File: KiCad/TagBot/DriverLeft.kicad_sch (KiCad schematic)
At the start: 3 parts, among them U2 ZXBM5210-SP

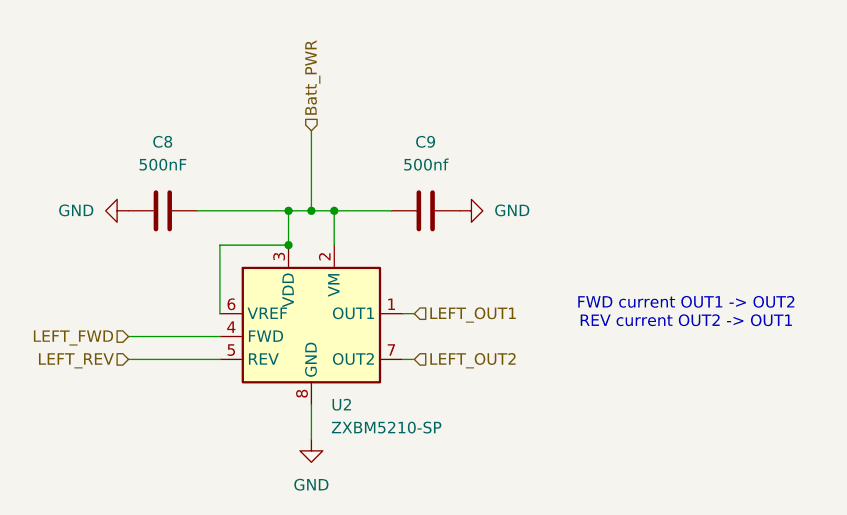
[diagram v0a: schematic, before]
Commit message: boot0 of stm32 connected to gnd
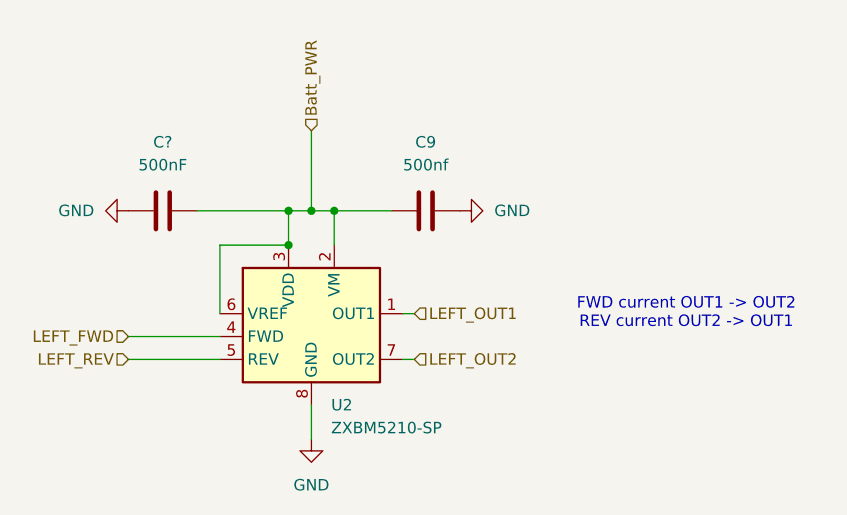
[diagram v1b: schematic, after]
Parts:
- renumbered C8 to C?
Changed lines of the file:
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@@
 		(dnp no)
 		(fields_autoplaced yes)
-		(property "Reference" "C8"
+		(property "Reference" "C?"
 			(at 124.46 66.04 90)
 			(effects
@@
 		)
 		(pin "1"
+		)
+		(instances
+			(project "TagBot"
+				(path "/6db08f37-7cb3-4000-93f1-ba0d0ffbeb19/3ab50834-de79-4373-bbc0-542f9f81e0c6"
+					(reference "C?")
+					(unit 1)
+				)
+			)
 		)
 	)
@@
 		(dnp no)
 		(fields_autoplaced yes)
-		(property "Reference" "#PWR019"
+		(property "Reference" "#PWR?"
 			(at 140.97 105.41 0)
 			(effects
@@
 		(pin "1"
 		)
-	)
+		(instances
+			(project "TagBot"
+				(path "/6db08f37-7cb3-4000-93f1-ba0d0ffbeb19/3ab50834-de79-4373-bbc0-542f9f81e0c6"
+					(reference "#PWR?")
+					(unit 1)
+				)
+			)
+		)
+	)

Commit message: update kicad
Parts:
- gave numbers to parts that had none: 1
- renumbered C9 to C202, U2 to U201
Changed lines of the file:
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@@
 	(generator "eeschema")
 	(generator_version "8.0")
-	(paper "A4")
+	(paper "A3")
 	(junction
 		(at 138.43 73.66)
@@
 		(dnp no)
 		(fields_autoplaced yes)
-		(property "Reference" "#PWR021"
+		(property "Reference" "#PWR0203"
 			(at 163.83 73.66 0)
 			(effects
@@
 			(project "TagBot"
 				(path "/6db08f37-7cb3-4000-93f1-ba0d0ffbeb19/3ab50834-de79-4373-bbc0-542f9f81e0c6"
-					(reference "#PWR021")
+					(reference "#PWR0203")
 					(unit 1)
 				)
@@
 		(dnp no)
 		(fields_autoplaced yes)
-		(property "Reference" "C?"
+		(property "Reference" "C201"
 			(at 124.46 66.04 90)
 			(effects
@@
 			(project "TagBot"
 				(path "/6db08f37-7cb3-4000-93f1-ba0d0ffbeb19/3ab50834-de79-4373-bbc0-542f9f81e0c6"
-					(reference "C?")
+					(reference "C201")
 					(unit 1)
 				)
@@
 		(dnp no)
 		(fields_autoplaced yes)
-		(property "Reference" "U2"
+		(property "Reference" "U201"
 			(at 143.1641 95.25 0)
 			(effects
@@
 			(project "TagBot"
 				(path "/6db08f37-7cb3-4000-93f1-ba0d0ffbeb19/3ab50834-de79-4373-bbc0-542f9f81e0c6"
-					(reference "U2")
+					(reference "U201")
 					(unit 1)
 				)
@@
 		(dnp no)
 		(fields_autoplaced yes)
-		(property "Reference" "#PWR020"
+		(property "Reference" "#PWR0201"
 			(at 114.3 73.66 0)
 			(effects
@@
 			(project "TagBot"
 				(path "/6db08f37-7cb3-4000-93f1-ba0d0ffbeb19/3ab50834-de79-4373-bbc0-542f9f81e0c6"
-					(reference "#PWR020")
+					(reference "#PWR0201")
 					(unit 1)
 				)
@@
 		(dnp no)
 		(fields_autoplaced yes)
-		(property "Reference" "C9"
+		(property "Reference" "C202"
 			(at 153.67 66.04 90)
 			(effects
@@
 			(project "TagBot"
 				(path "/6db08f37-7cb3-4000-93f1-ba0d0ffbeb19/3ab50834-de79-4373-bbc0-542f9f81e0c6"
-					(reference "C9")
+					(reference "C202")
 					(unit 1)
 				)
@@
 		(dnp no)
 		(fields_autoplaced yes)
-		(property "Reference" "#PWR?"
+		(property "Reference" "#PWR0202"
 			(at 140.97 105.41 0)
 			(effects
@@
 			(project "TagBot"
 				(path "/6db08f37-7cb3-4000-93f1-ba0d0ffbeb19/3ab50834-de79-4373-bbc0-542f9f81e0c6"
-					(reference "#PWR?")
+					(reference "#PWR0202")
 					(unit 1)
 				)

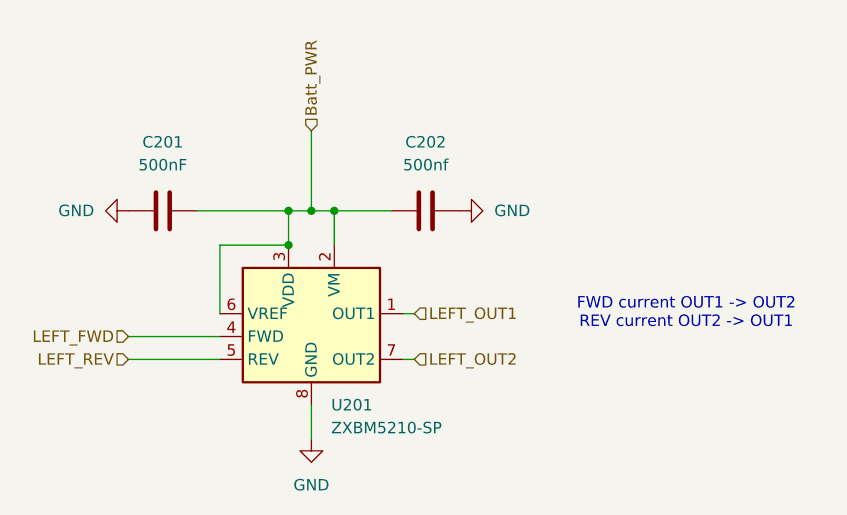
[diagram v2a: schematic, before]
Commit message: update footprint kicad
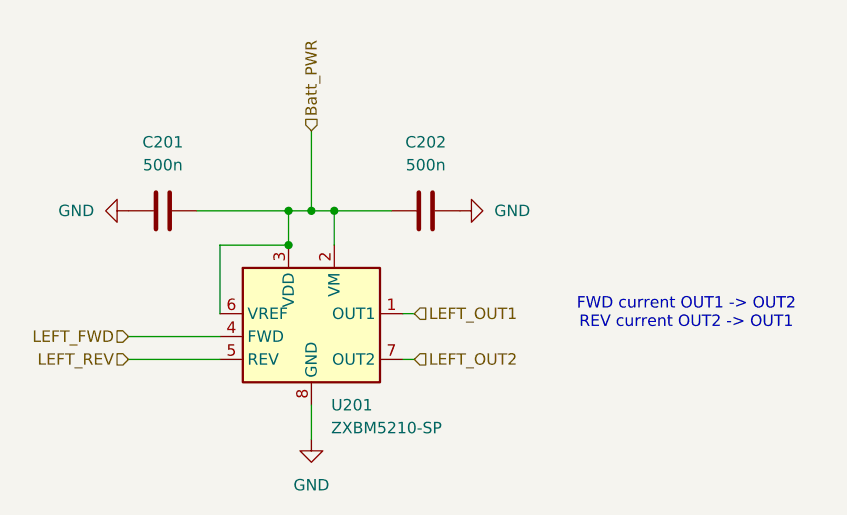
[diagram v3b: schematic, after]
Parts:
- C201: value 500nF -> 500n; footprint (none) -> Capacitor_SMD:C_0402_1005Metric
- C202: value 500nf -> 500n; footprint (none) -> Capacitor_SMD:C_0402_1005Metric
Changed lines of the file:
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@@
 			)
 		)
-		(property "Value" "500nF"
+		(property "Value" "500n"
 			(at 124.46 68.58 90)
 			(effects
@@
 			)
 		)
-		(property "Footprint" ""
+		(property "Footprint" "Capacitor_SMD:C_0402_1005Metric"
 			(at 128.27 72.6948 0)
 			(effects
@@
 			)
 		)
-		(property "Value" "500nf"
+		(property "Value" "500n"
 			(at 153.67 68.58 90)
 			(effects
@@
 			)
 		)
-		(property "Footprint" ""
+		(property "Footprint" "Capacitor_SMD:C_0402_1005Metric"
 			(at 149.86 74.6252 0)
 			(effects

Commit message: placement pcb
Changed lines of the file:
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@@
 		(color 0 0 0 0)
 	)
+	(junction
+		(at 143.51 76.2)
+		(diameter 0)
+		(color 0 0 0 0)
+	)
+	(wire
+		(pts
+			(xy 144.78 76.2) (xy 143.51 76.2)
+		)
+		(stroke
+			(width 0)
+			(type default)
+		)
+	)
 	(wire
 		(pts
@@
 	(wire
 		(pts
-			(xy 143.51 73.66) (xy 143.51 77.47)
+			(xy 143.51 73.66) (xy 143.51 76.2)
 		)
 		(stroke
@@
 		(pts
 			(xy 149.86 73.66) (xy 143.51 73.66)
+		)
+		(stroke
+			(width 0)
+			(type default)
+		)
+	)
+	(wire
+		(pts
+			(xy 143.51 76.2) (xy 143.51 77.47)
 		)
 		(stroke
@@
 					(unit 1)
 				)
+			)
+		)
+	)
+	(symbol
+		(lib_id "power:PWR_FLAG")
+		(at 144.78 76.2 270)
+		(unit 1)
+		(exclude_from_sim no)
+		(in_bom yes)
+		(on_board yes)
+		(dnp no)
+		(fields_autoplaced yes)
+		(property "Reference" "#FLG0201"
+			(at 146.685 76.2 0)
+			(effects
+				(font
+					(size 1.27 1.27)
+				)
+				(hide yes)
+			)
+		)
+		(property "Value" "PWR_FLAG"
+			(at 148.59 76.1999 90)
+			(effects
+				(font
+					(size 1.27 1.27)
+				)
+				(justify left)
+			)
+		)
+		(property "Footprint" ""
+			(at 144.78 76.2 0)
+			(effects
+				(font
+					(size 1.27 1.27)
+				)
+				(hide yes)
+			)
+		)
+		(property "Datasheet" "~"
+			(at 144.78 76.2 0)
+			(effects
+				(font
+					(size 1.27 1.27)
+				)
+				(hide yes)
+			)
+		)
+		(property "Description" "Special symbol for telling ERC where power comes from"
+			(at 144.78 76.2 0)
+			(effects
+				(font
+					(size 1.27 1.27)
+				)
+				(hide yes)
+			)
+		)
+		(pin "1"
+		)
+		(instances
+			(project ""
+				(path "/6db08f37-7cb3-4000-93f1-ba0d0ffbeb19/3ab50834-de79-4373-bbc0-542f9f81e0c6"
+					(reference "#FLG0201")
+					(unit 1)
+				)

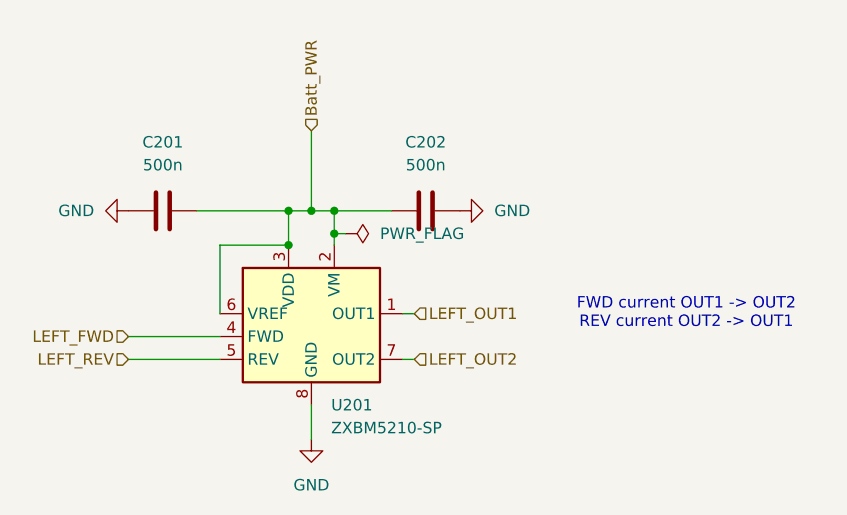
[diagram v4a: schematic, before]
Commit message: correction schema kicad
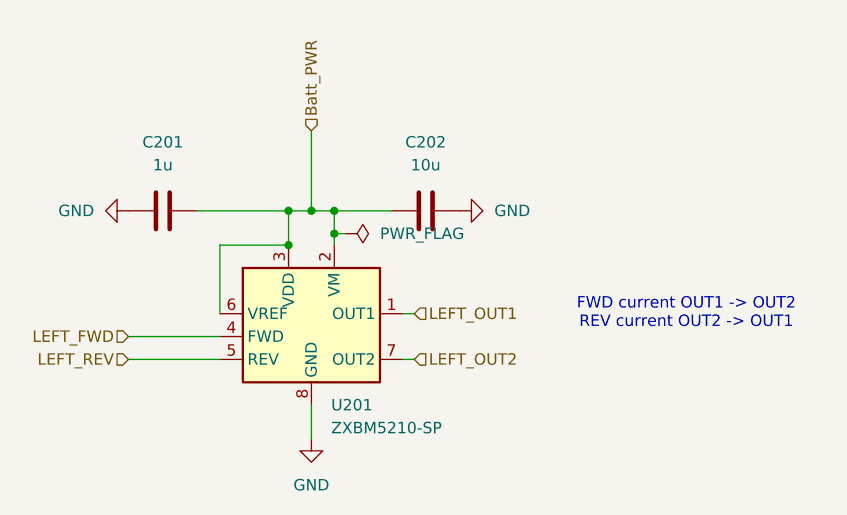
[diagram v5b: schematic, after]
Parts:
- C201: value 500n -> 1u
- C202: value 500n -> 10u
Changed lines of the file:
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@@
 			)
 		)
-		(property "Value" "500n"
+		(property "Value" "1u"
 			(at 124.46 68.58 90)
 			(effects
@@
 			)
 		)
-		(property "Value" "500n"
+		(property "Value" "10u"
 			(at 153.67 68.58 90)
 			(effects

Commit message: update routage
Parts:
- added TP1, TP2: TestPoint, TestPoint:TestPoint_Pad_D1.5mm, symbol Connector:TestPoint
- C201, C202: footprint Capacitor_SMD:C_0402_1005Metric -> Capacitor_SMD:C_0603_1608Metric
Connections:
- net LEFT_FWD: now also TP1.1
- net LEFT_REV: now also TP2.1
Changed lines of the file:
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@@
 		(color 0 0 0 0)
 	)
+	(junction
+		(at 123.19 90.17)
+		(diameter 0)
+		(color 0 0 0 0)
+	)
+	(junction
+		(at 123.19 87.63)
+		(diameter 0)
+		(color 0 0 0 0)
+	)
 	(wire
 		(pts
@@
 	(wire
 		(pts
+			(xy 123.19 87.63) (xy 130.81 87.63)
+		)
+		(stroke
+			(width 0)
+			(type default)
+		)
+	)
+	(wire
+		(pts
 			(xy 138.43 77.47) (xy 138.43 73.66)
 		)
@@
 	(wire
 		(pts
-			(xy 120.65 90.17) (xy 130.81 90.17)
+			(xy 120.65 90.17) (xy 123.19 90.17)
 		)
 		(stroke
@@
 	(wire
 		(pts
+			(xy 123.19 90.17) (xy 130.81 90.17)
+		)
+		(stroke
+			(width 0)
+			(type default)
+		)
+	)
+	(wire
+		(pts
 			(xy 149.86 73.66) (xy 143.51 73.66)
 		)
@@
 	(wire
 		(pts
-			(xy 120.65 87.63) (xy 130.81 87.63)
+			(xy 120.65 87.63) (xy 123.19 87.63)
 		)
 		(stroke
@@
 			)
 			(justify left)
+		)
+	)
+	(symbol
+		(lib_id "Connector:TestPoint")
+		(at 123.19 90.17 180)
+		(unit 1)
+		(exclude_from_sim no)
+		(in_bom yes)
+		(on_board yes)
+		(dnp no)
+		(fields_autoplaced yes)
+		(property "Reference" "TP2"
+			(at 125.73 92.2019 0)
+			(effects
+				(font
+					(size 1.27 1.27)
+				)
+				(justify right)
+			)
+		)
+		(property "Value" "TestPoint"
+			(at 125.73 94.7419 0)
+			(effects
+				(font
+					(size 1.27 1.27)
+				)
+				(justify right)
+			)
+		)
+		(property "Footprint" "TestPoint:TestPoint_Pad_D1.5mm"
+			(at 118.11 90.17 0)
+			(effects
+				(font
+					(size 1.27 1.27)
+				)
+				(hide yes)
+			)
+		)
+		(property "Datasheet" "~"
+			(at 118.11 90.17 0)
+			(effects
+				(font
+					(size 1.27 1.27)
+				)
+				(hide yes)
+			)
+		)
+		(property "Description" "test point"
+			(at 123.19 90.17 0)
+			(effects
+				(font
+					(size 1.27 1.27)
+				)
+				(hide yes)
+			)
+		)
+		(pin "1"
+		)
+		(instances
+			(project "TagBot"
+				(path "/6db08f37-7cb3-4000-93f1-ba0d0ffbeb19/3ab50834-de79-4373-bbc0-542f9f81e0c6"
+					(reference "TP2")
+					(unit 1)
+				)
+			)
 		)
 	)
@@
 			)
 		)
-		(property "Footprint" "Capacitor_SMD:C_0402_1005Metric"
+		(property "Footprint" "Capacitor_SMD:C_0603_1608Metric"
 			(at 128.27 72.6948 0)
 			(effects
@@
 	)
 	(symbol
+		(lib_id "Connector:TestPoint")
+		(at 123.19 87.63 0)
+		(unit 1)
+		(exclude_from_sim no)
+		(in_bom yes)
+		(on_board yes)
+		(dnp no)
+		(fields_autoplaced yes)
+		(property "Reference" "TP1"
+			(at 125.73 83.0579 0)
+			(effects
+				(font
+					(size 1.27 1.27)
+				)
+				(justify left)
+			)
+		)
+		(property "Value" "TestPoint"
+			(at 125.73 85.5979 0)
+			(effects
+				(font
+					(size 1.27 1.27)
+				)
+				(justify left)
+			)
+		)
+		(property "Footprint" "TestPoint:TestPoint_Pad_D1.5mm"
+			(at 128.27 87.63 0)
+			(effects
+				(font
+					(size 1.27 1.27)
+				)
+				(hide yes)
+			)
+		)
+		(property "Datasheet" "~"
+			(at 128.27 87.63 0)
+			(effects
+				(font
+					(size 1.27 1.27)
+				)
+				(hide yes)
+			)
+		)
+		(property "Description" "test point"
+			(at 123.19 87.63 0)
+			(effects
+				(font
+					(size 1.27 1.27)
+				)
+				(hide yes)
+			)
+		)
+		(pin "1"
+		)
+		(instances
+			(project ""
+				(path "/6db08f37-7cb3-4000-93f1-ba0d0ffbeb19/3ab50834-de79-4373-bbc0-542f9f81e0c6"
+					(reference "TP1")
+					(unit 1)
+				)
+			)
+		)
+	)
+	(symbol
 		(lib_id "Device:C")
 		(at 153.67 73.66 270)
@@
 			)
 		)
-		(property "Footprint" "Capacitor_SMD:C_0402_1005Metric"
+		(property "Footprint" "Capacitor_SMD:C_0603_1608Metric"
 			(at 149.86 74.6252 0)
 			(effects

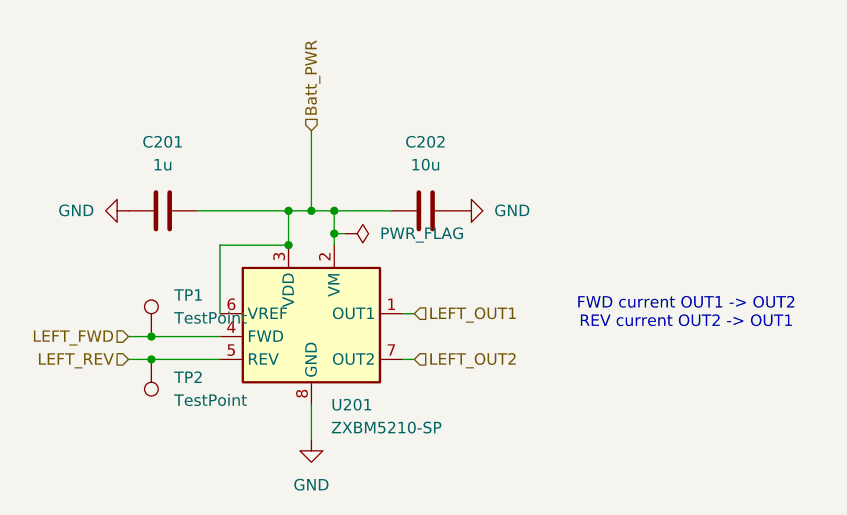
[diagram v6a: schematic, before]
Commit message: fixed switch footprint and genrated gerber files
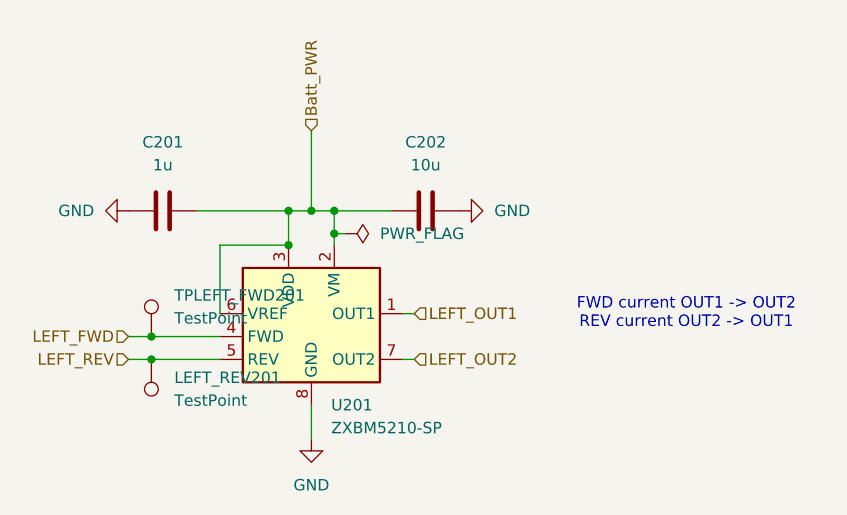
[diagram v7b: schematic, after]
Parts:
- renumbered TP2 to LEFT_REV201, TP1 to TPLEFT_FWD201
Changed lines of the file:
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@@
 		(dnp no)
 		(fields_autoplaced yes)
-		(property "Reference" "TP2"
+		(property "Reference" "LEFT_REV201"
 			(at 125.73 92.2019 0)
 			(effects
@@
 			(project "TagBot"
 				(path "/6db08f37-7cb3-4000-93f1-ba0d0ffbeb19/3ab50834-de79-4373-bbc0-542f9f81e0c6"
-					(reference "TP2")
+					(reference "LEFT_REV201")
 					(unit 1)
 				)
@@
 		(dnp no)
 		(fields_autoplaced yes)
-		(property "Reference" "TP1"
+		(property "Reference" "TPLEFT_FWD201"
 			(at 125.73 83.0579 0)
 			(effects
@@
 			(project ""
 				(path "/6db08f37-7cb3-4000-93f1-ba0d0ffbeb19/3ab50834-de79-4373-bbc0-542f9f81e0c6"
-					(reference "TP1")
-					(unit 1)
-				)
+					(reference "TPLEFT_FWD201")
+					(unit 1)
+				)
